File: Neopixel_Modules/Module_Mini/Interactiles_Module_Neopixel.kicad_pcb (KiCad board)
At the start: 4 copper layers, 37.8 x 33.1 mm, 33 parts, among them J1 PINHD_1x2_Male, J2 PINHD_1x2_Female, J3 PINHD_1x2_Female, J4 PINHD_1x2_Female, J6 PINHD_1x2_Female, J8 PINHD_1x2_Female, U1 MCP23017_ML

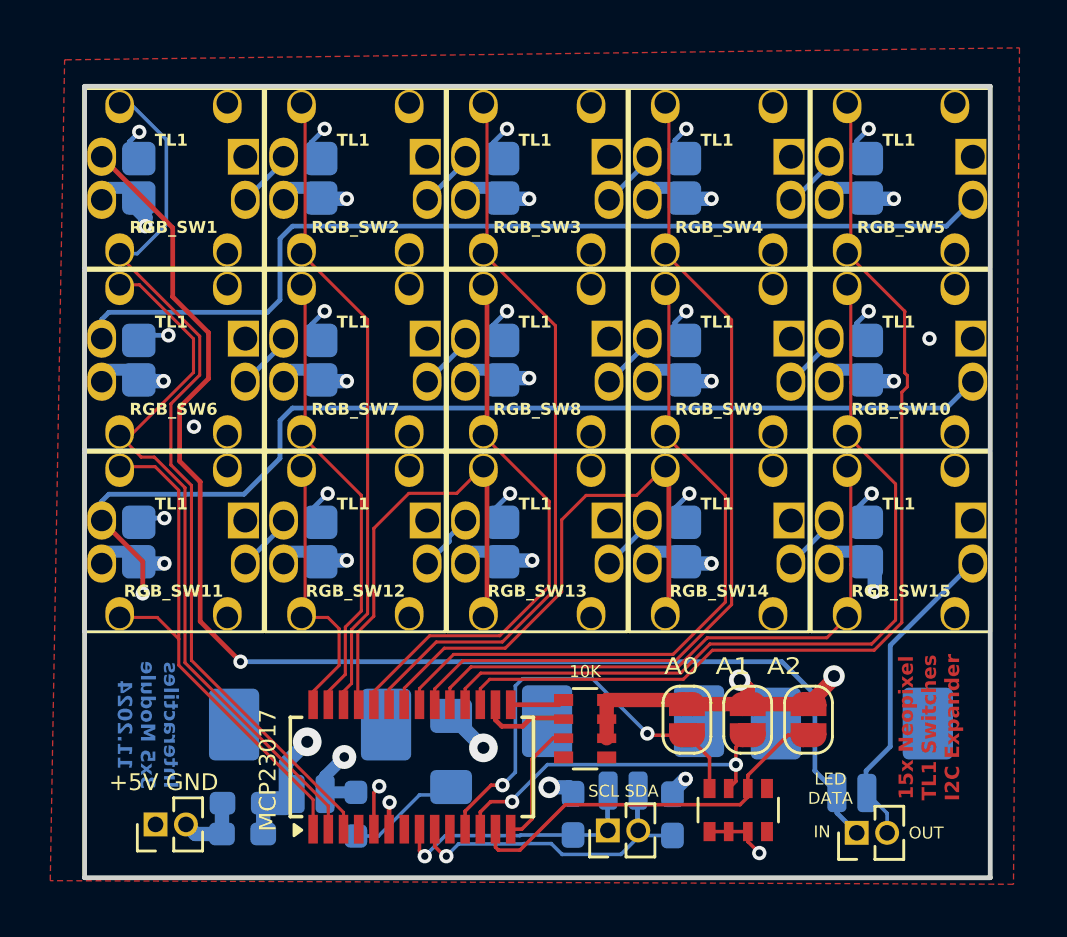
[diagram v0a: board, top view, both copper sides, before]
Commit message: replaced picoblade connectors with THT pads, moved some stuff around
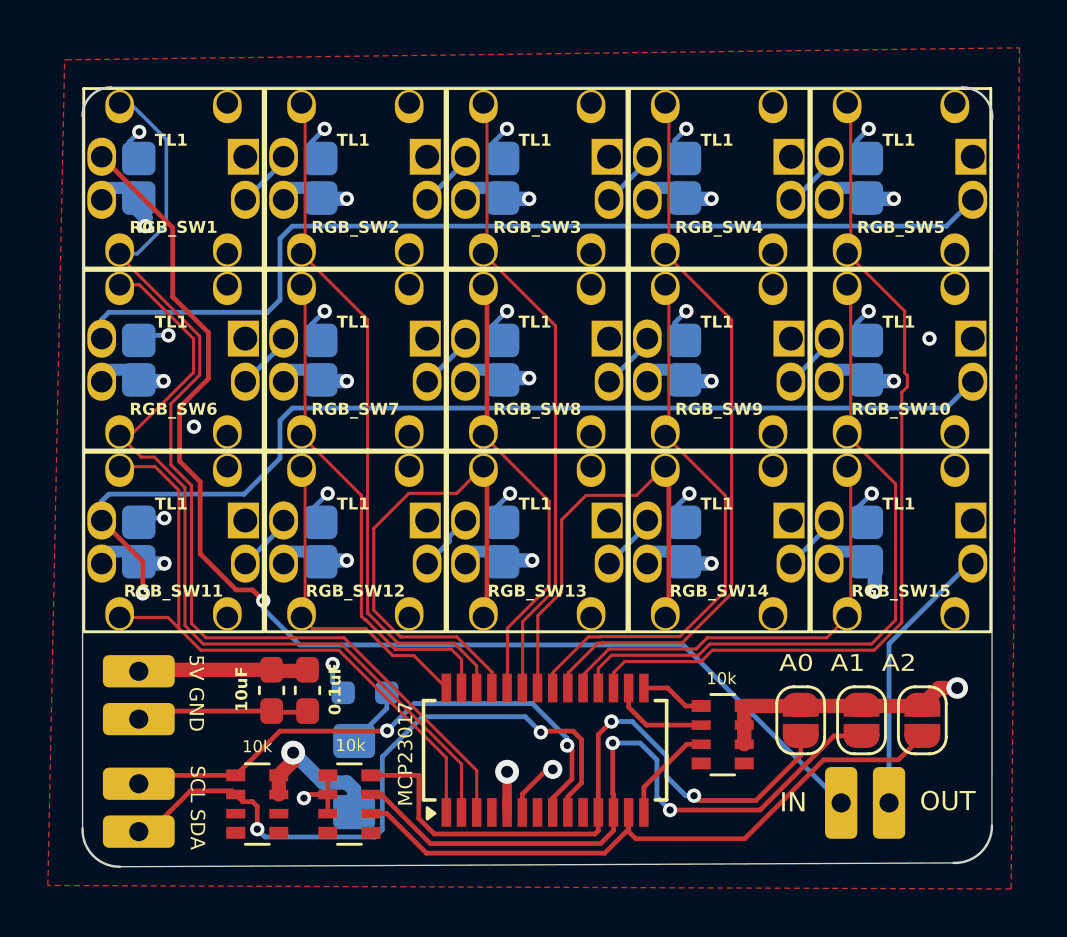
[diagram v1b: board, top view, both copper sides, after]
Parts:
- removed J3, J6, J8: PINHD_1x2_Female, Connector_PinHeader_1.27mm:PinHeader_1x02_P1.27mm_Vertical
- removed LED: LED, LED_SMD:LED_1206_3216Metric_Pad1.42x1.75mm_HandSolder
- removed R2, R3: 10k, Capacitor_SMD:C_0603_1608Metric_Pad1.08x0.95mm_HandSolder
- added 10k: R_Pack04, Resistor_SMD:R_Array_Convex_4x0603, F.Cu at (112.4, 86.2)
- added D1: LED, LED_SMD:LED_1206_3216Metric_Pad1.42x1.75mm_HandSolder, B.Cu at (116.5, 85.0)
- C1, C2: moved to F.Cu
- J1, J2, J4: footprint Connector_Molex:Molex_PicoBlade_53261-0271_1x02-1MP_P1.25mm_Horizontal -> Connector_PinHeader_2.00mm:PinHeader_1x02_P2.00mm_Vertical
- R1: value 10k -> 330ohm
- moved J2 20.3 mm to (107.5, 85.3), turned to 180 degrees
- moved 10k 16.3 mm to (116.3, 86.2), turned to 0 degrees
- moved J1 7.66 mm to (107.5, 80.6), turned to 180 degrees
- moved C1 6.12 mm to (113.0, 81.4), turned to -90 degrees
- moved RN2 5.76 mm to (131.9, 83.3)
- moved U1 5.61 mm to (124.4, 83.9)
- moved C2 5.43 mm to (114.5, 81.4), turned to -90 degrees
- moved R1 5.08 mm to (116.9, 81.5), turned to 180 degrees
- moved JP2 4.75 mm to (137.7, 82.7)
- moved JP3 4.75 mm to (140.2, 82.7)
- moved JP1 4.75 mm to (135.1, 82.7)
- moved J4 2.85 mm to (136.8, 86.1), turned to -90 degrees
- renumbered RN1 to 10k
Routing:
- net Net-(JP2-A): track 14.8 -> 28.6 mm
- net SDA: track 15.2 -> 28.1 mm, vias 1 -> 2
- net SCL: track 11.0 -> 23.4 mm, vias 1 -> 2
- net Net-(JP3-A): track 16.4 -> 27.5 mm
- net Net-(JP1-A): track 18.0 -> 27.8 mm
- net SW15: track 25.0 -> 18.4 mm
- net SW4: track 36.8 -> 30.6 mm
- net SW9: track 29.4 -> 23.2 mm
- net SW5: track 42.4 -> 36.6 mm
- net SW10: track 34.8 -> 29.0 mm
- net SW6: track 30.0 -> 35.0 mm
- net LED_IN: track 55.6 -> 50.6 mm
- net SW11: track 22.2 -> 27.1 mm
- net SW1: track 37.5 -> 42.4 mm
- net SW8: track 23.6 -> 18.7 mm
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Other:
- board size 37.8 x 33.1 mm -> 38 x 32.6 mm
- board text added: "10k"
- board text added: "5V GND"
- board text removed: "+5V GND"
- board text removed: "10K"
- board text removed: "15x Neopixel TL1 Switches I2C Expander"
- board text removed: "LED DATA"

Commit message: fixed for pcb production
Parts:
- R1: value 330ohm -> 330R
- moved R1 0.50 mm to (116.4, 81.5)
- moved 10k 0.25 mm to (112.7, 86.2)
- renumbered D1 to LED
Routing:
- net Net-(RGB_SW11-DIN): track 44.1 -> 40.4 mm, vias 1 -> 0
- net SW6: track 35.0 -> 32.3 mm
- net SDA: track 28.1 -> 25.5 mm
- net GND: track 35.1 -> 37.4 mm, vias 20 -> 18
- net SW11: track 27.1 -> 25.3 mm
- net Net-(JP1-A): track 27.8 -> 26.8 mm
- net LED_IN: track 50.6 -> 50.0 mm
